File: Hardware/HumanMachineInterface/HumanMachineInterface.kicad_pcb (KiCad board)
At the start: 2 copper layers, 85 x 60 mm, 22 parts, among them Q1 Q_Photo_NPN, SW1 SW_Push, SW2 SW_Push, SW3 SW_Push, SW4 SW_Push, U2 ST7735S

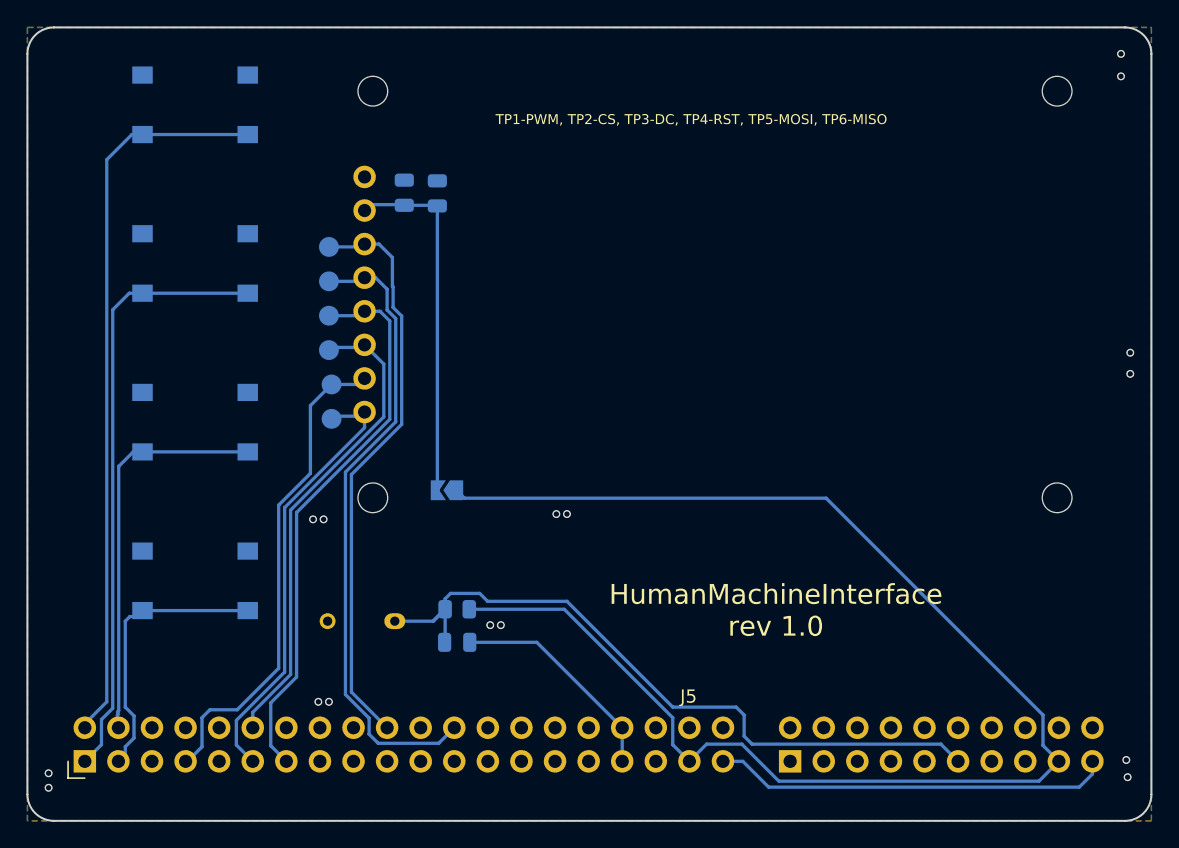
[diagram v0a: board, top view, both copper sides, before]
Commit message: make boards smaller, fix sd card slot
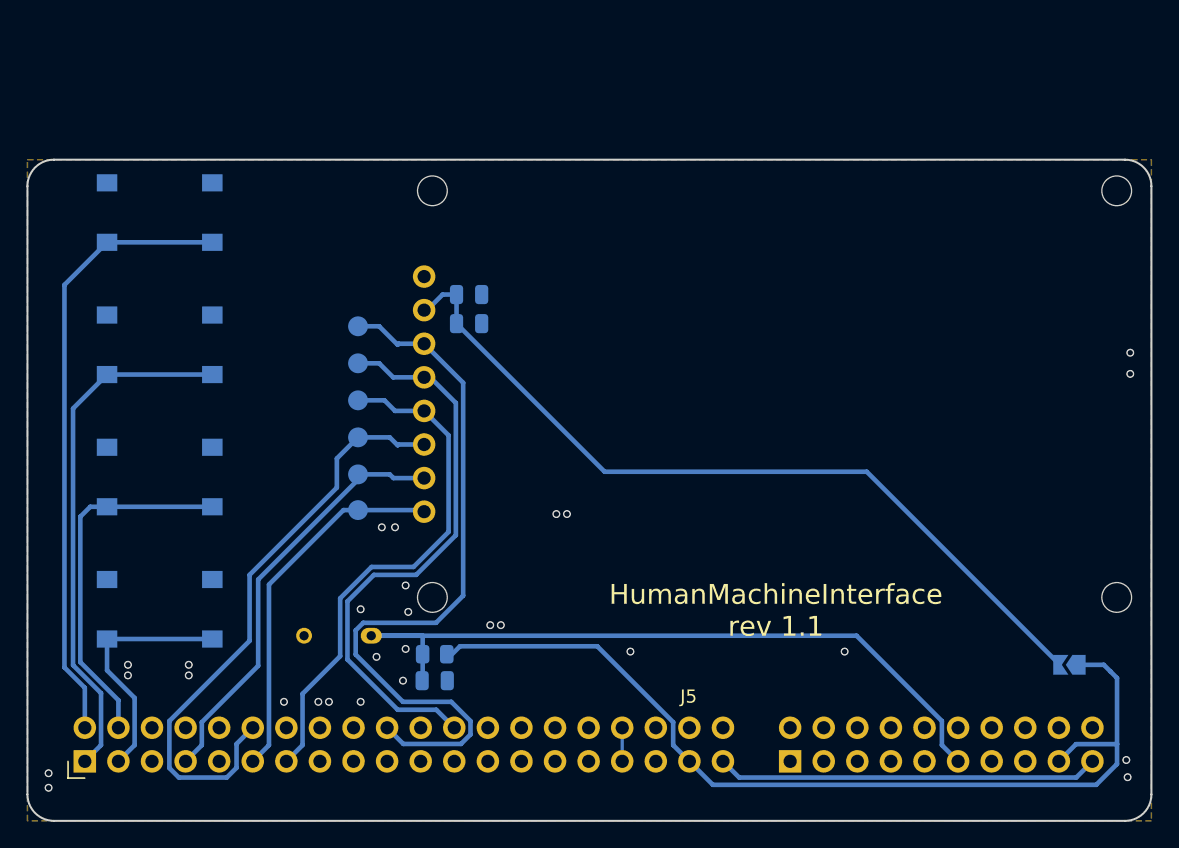
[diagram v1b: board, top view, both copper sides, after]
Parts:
- moved JP1 48.9 mm to (208.8, 108.2)
- moved C2 11.0 mm to (163.4, 82.4), turned to 0 degrees
- moved U2 8.78 mm to (158.5, 70.2)
- moved SW1 8.58 mm to (140.0, 74.0)
- moved G*** 8.44 mm to (132.5, 74.0)
- moved C1 8.02 mm to (163.4, 80.2), turned to 0 degrees
- moved TP1 7.18 mm to (155.0, 96.5)
- moved TP2 7.09 mm to (155.0, 93.8)
- moved TP3 6.96 mm to (155.0, 91.0)
- moved TP4 6.77 mm to (155.0, 88.2)
- moved SW2 6.71 mm to (140.0, 84.0)
- moved TP5 6.58 mm to (155.0, 85.4)
- moved G*** 6.52 mm to (132.5, 84.0)
- moved TP6 6.39 mm to (155.0, 82.6)
- moved SW3 4.94 mm to (140.0, 94.0)
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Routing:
- net 3V3_FROM_MAINBOARD: track 108.3 -> 71.6 mm
- net Net-(JP1-B): track 26.5 -> 61.5 mm
- net GND: track 16.7 -> 2.54 mm, vias 16 -> 23
- net SPI1_SCK: track 43.5 -> 55.8 mm
- net GPIO_5: track 35.6 -> 45.4 mm
- net GPIO_15: track 54.8 -> 46.6 mm
- net GPIO_16: track 45.8 -> 39.7 mm
- net GPIO_6: track 32.9 -> 28.0 mm
- net SPI1_MOSI: track 47.9 -> 43.5 mm
- net GPIO_10: track 36.3 -> 32.2 mm
- net GPIO_4: track 42.1 -> 39.5 mm
- net GPIO_18: track 54.3 -> 56.8 mm
- net GPIO_13: track 29.9 -> 27.4 mm
- net GPIO_14: track 20.3 -> 18.6 mm
- net 5V: track 30.1 -> 29.0 mm
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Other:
- board size 85 x 60 mm -> 85 x 50 mm
- board text added: "HumanMachineInterface rev 1.1"
- board text removed: "HumanMachineInterface rev 1.0"

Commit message: xx
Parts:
- SW1, SW2, SW3, SW4: footprint Button_Switch_SMD:SW_SPST_PTS645 -> Button_Switch_SMD:SW_SPST_PTS645Sx43SMTR92
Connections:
- J5 pad 13: GPIO_4 -> unconnected-(J5-Pin_13-Pad13)
- J5 pad 5: unconnected-(J5-Pin_5-Pad5) -> GPIO_12
- J5 pad 7: GPIO_10 -> unconnected-(J5-Pin_7-Pad7)
- J5 pad 9: unconnected-(J5-Pin_9-Pad9) -> GPIO_8
- TP2 pad 1: GPIO_10 -> GPIO_12
- TP4 pad 1: GPIO_4 -> GPIO_8
- U2 pad 5: GPIO_4 -> GPIO_8
- U2 pad 7: GPIO_10 -> GPIO_12
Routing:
- net GPIO_8: track 0.00 -> 48.6 mm
- net GPIO_4: track 39.5 -> 0.00 mm
- net GPIO_12: track 0.00 -> 34.9 mm, vias 0 -> 2
- net GPIO_10: track 32.2 -> 0.00 mm
- net GPIO_5: track 45.4 -> 32.4 mm
- net SPI1_MOSI: track 43.5 -> 42.4 mm
- net GND: vias 23 -> 33
- net (no net): vias 5 -> 2
